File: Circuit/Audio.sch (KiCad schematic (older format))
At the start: 12 parts, among them U5 NAU8814

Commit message: BOM information to schematic. Power & main sheets mostly.
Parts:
- renumbered C17 to C?, C10 to C?
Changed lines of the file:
@@
 	1400 3900 1550 3900
 $Comp
-L C_Small C17
+L C_Small C?
 U 1 1 581FF4BD
 P 6950 3250
-F 0 "C17" H 6960 3320 50  0000 L CNN
+F 0 "C?" H 6960 3320 50  0000 L CNN
 F 1 "100pF" H 6960 3170 50  0000 L CNN
 F 2 "Capacitors_SMD:C_0603_HandSoldering" H 6950 3250 50  0001 C CNN
@@
 $EndComp
 $Comp
-L C_Small C10
+L C_Small C?
 U 1 1 5820032A
 P 6500 3000
-F 0 "C10" H 6510 3070 50  0000 L CNN
+F 0 "C?" H 6510 3070 50  0000 L CNN
 F 1 "100pF" H 6510 2920 50  0000 L CNN
 F 2 "Capacitors_SMD:C_0603_HandSoldering" H 6500 3000 50  0001 C CNN

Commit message: Updated alligator clips.
Some basic placement
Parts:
- gave numbers to parts that had none: 2
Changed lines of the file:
@@
 Connection ~ 1400 2450
 $Comp
-L +3.3V #PWR059
+L +3.3V #PWR056
 U 1 1 581BE27A
 P 5750 2750
-F 0 "#PWR059" H 5750 2600 50  0001 C CNN
+F 0 "#PWR056" H 5750 2600 50  0001 C CNN
 F 1 "+3.3V" H 5750 2890 50  0000 C CNN
 F 2 "" H 5750 2750 50  0000 C CNN
@@
 	2100 1900 2250 1900
 $Comp
-L GND #PWR060
+L GND #PWR057
 U 1 1 581BEFAA
 P 5750 2200
-F 0 "#PWR060" H 5750 1950 50  0001 C CNN
+F 0 "#PWR057" H 5750 1950 50  0001 C CNN
 F 1 "GND" H 5750 2050 50  0000 C CNN
 F 2 "" H 5750 2200 50  0000 C CNN
@@
 	800  2450 800  2050
 $Comp
-L GND #PWR061
+L GND #PWR058
 U 1 1 581BF41C
 P 7400 3850
-F 0 "#PWR061" H 7400 3600 50  0001 C CNN
+F 0 "#PWR058" H 7400 3600 50  0001 C CNN
 F 1 "GND" H 7400 3700 50  0000 C CNN
 F 2 "" H 7400 3850 50  0000 C CNN
@@
 Mono Out - NC or come out to header?\nOr could go to TRS 3.5mm jack.
 $Comp
-L GND #PWR062
+L GND #PWR059
 U 1 1 581BFD59
 P 4600 4450
-F 0 "#PWR062" H 4600 4200 50  0001 C CNN
+F 0 "#PWR059" H 4600 4200 50  0001 C CNN
 F 1 "GND" H 4600 4300 50  0000 C CNN
 F 2 "" H 4600 4450 50  0000 C CNN
@@
 Connection ~ 3850 3800
 $Comp
-L +3.3V #PWR063
+L +3.3V #PWR060
 U 1 1 581C0164
 P 3600 3600
-F 0 "#PWR063" H 3600 3450 50  0001 C CNN
+F 0 "#PWR060" H 3600 3450 50  0001 C CNN
 F 1 "+3.3V" H 3600 3740 50  0000 C CNN
 F 2 "" H 3600 3600 50  0000 C CNN
@@
 $EndComp
 $Comp
-L GND #PWR064
+L GND #PWR061
 U 1 1 581C01A1
 P 3850 4450
-F 0 "#PWR064" H 3850 4200 50  0001 C CNN
+F 0 "#PWR061" H 3850 4200 50  0001 C CNN
 F 1 "GND" H 3850 4300 50  0000 C CNN
 F 2 "" H 3850 4450 50  0000 C CNN
@@
 AUX input could go to DAC on ESP32..\nfor.. reasons?\nOr could go to TRS 3.5mm jack.
 $Comp
-L GND #PWR065
+L GND #PWR062
 U 1 1 581C0598
 P 5850 4700
-F 0 "#PWR065" H 5850 4450 50  0001 C CNN
+F 0 "#PWR062" H 5850 4450 50  0001 C CNN
 F 1 "GND" H 5850 4550 50  0000 C CNN
 F 2 "" H 5850 4700 50  0000 C CNN
@@
 	1400 3900 1550 3900
 $Comp
-L C_Small C?
+L C_Small C18
 U 1 1 581FF4BD
 P 6950 3250
-F 0 "C?" H 6960 3320 50  0000 L CNN
+F 0 "C18" H 6960 3320 50  0000 L CNN
 F 1 "100pF" H 6960 3170 50  0000 L CNN
 F 2 "Capacitors_SMD:C_0603_HandSoldering" H 6950 3250 50  0001 C CNN
@@
 $EndComp
 $Comp
-L C_Small C?
+L C_Small C17
 U 1 1 5820032A
 P 6500 3000
-F 0 "C?" H 6510 3070 50  0000 L CNN
+F 0 "C17" H 6510 3070 50  0000 L CNN
 F 1 "100pF" H 6510 2920 50  0000 L CNN
 F 2 "Capacitors_SMD:C_0603_HandSoldering" H 6500 3000 50  0001 C CNN

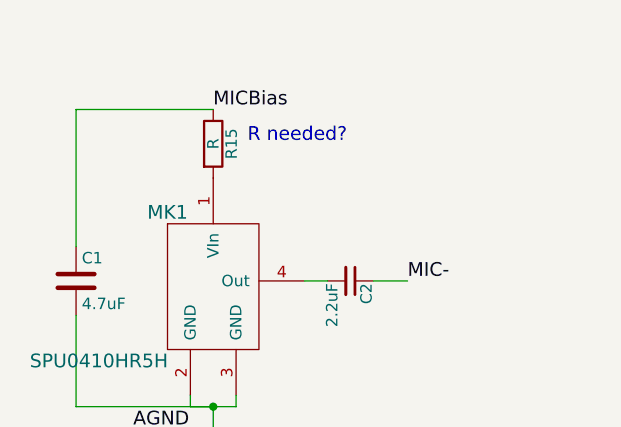
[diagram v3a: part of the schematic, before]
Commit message: Change to 3v3 regulator.
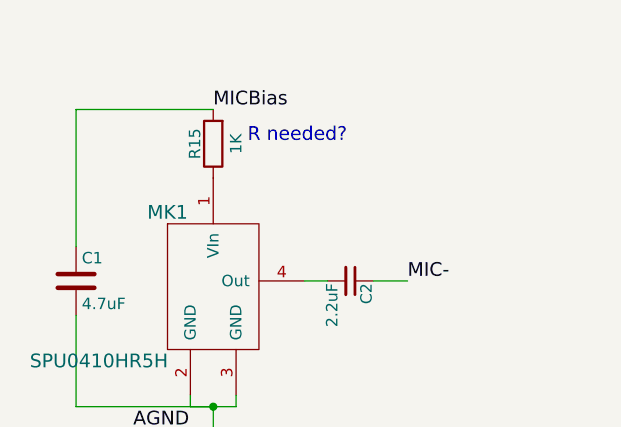
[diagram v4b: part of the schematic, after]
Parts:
- C2: footprint (none) -> Capacitors_SMD:C_0603_HandSoldering
- R15: value R -> 1K; footprint (none) -> Resistors_SMD:R_0603_HandSoldering; Digikey PN (none) -> 311-1.0KGRCT-ND; Link (none) -> http://www.digikey.com.au/product-detail/en/yageo/RC0603JR-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; Manufacturer PN (none) -> RC0603JR-071KL; Unit Cost (none) -> 0.10
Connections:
- net MICBias: now also R15.2; no longer R15.1
- net at MK1.1 (VIn): now also R15.1; no longer R15.2
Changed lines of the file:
@@
 LIBS:spu0410hr5h
 LIBS:ili9341.touchlcd.red
+LIBS:NCP5501
 LIBS:IoTuz-cache
 EELAYER 25 0
@@
 F 0 "C2" H 2010 1970 50  0000 L CNN
 F 1 "2.2uF" H 2010 1820 50  0000 L CNN
-F 2 "" H 2000 1900 50  0001 C CNN
+F 2 "Capacitors_SMD:C_0603_HandSoldering" H 2000 1900 50  0001 C CNN
 F 3 "" H 2000 1900 50  0000 C CNN
 F 4 "490-3296-1-ND" H 2000 1900 60  0001 C CNN "Digikey PN"
@@
 Text Label 1400 1150 0    60   ~ 0
 MICBias
-$Comp
-L R R15
-U 1 1 581BC437
-P 1400 1300
-F 0 "R15" V 1480 1300 50  0000 C CNN
-F 1 "R" V 1400 1300 50  0000 C CNN
-F 2 "" V 1330 1300 50  0001 C CNN
-F 3 "" H 1400 1300 50  0000 C CNN
-	1    1400 1300
-	1    0    0    -1
-$EndComp
 Wire Wire Line
 	5450 2700 5450 2900
@@
 Connection ~ 6500 3500
 Connection ~ 6500 3250
+$Comp
+L R R15
+U 1 1 5824B8C8
+P 1400 1300
+F 0 "R15" V 1480 1300 50  0000 C CNN
+F 1 "1K" V 1300 1300 50  0000 C CNN
+F 2 "Resistors_SMD:R_0603_HandSoldering" V 1330 1300 50  0001 C CNN
+F 3 "" H 1400 1300 50  0000 C CNN
+F 4 "311-1.0KGRCT-ND" V 1400 1300 60  0001 C CNN "Digikey PN"
+F 5 "http://www.digikey.com.au/product-detail/en/yageo/RC0603JR-071KL/311-1.0KGRCT-ND/729624" V 1400 1300 60  0001 C CNN "Link"
+F 6 "RC0603JR-071KL" V 1400 1300 60  0001 C CNN "Manufacturer PN"
+F 7 "0.10" V 1400 1300 60  0001 C CNN "Unit Cost"
+	1    1400 1300
+	-1   0    0    1
+$EndComp
 $EndSCHEMATC

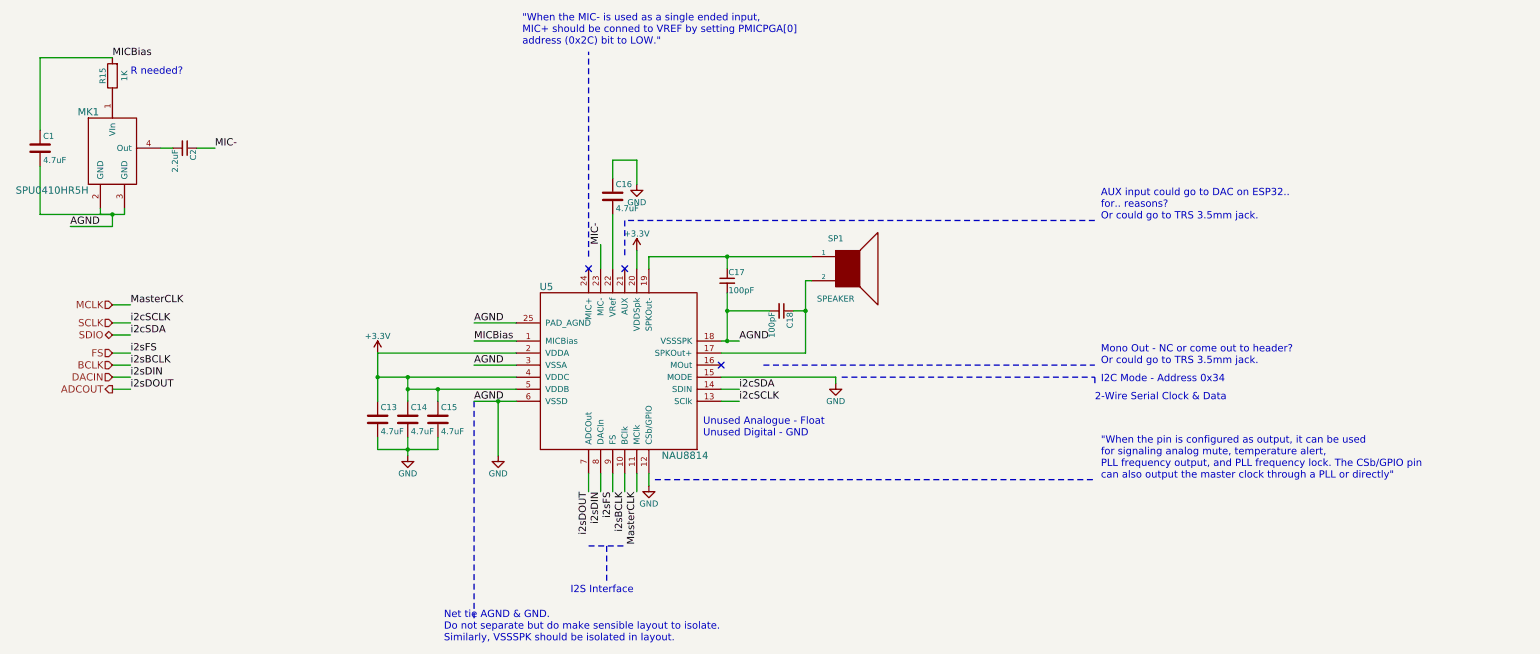
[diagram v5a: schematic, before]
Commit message: Changes to audio. Added 3.5mm TRS jack footprint.
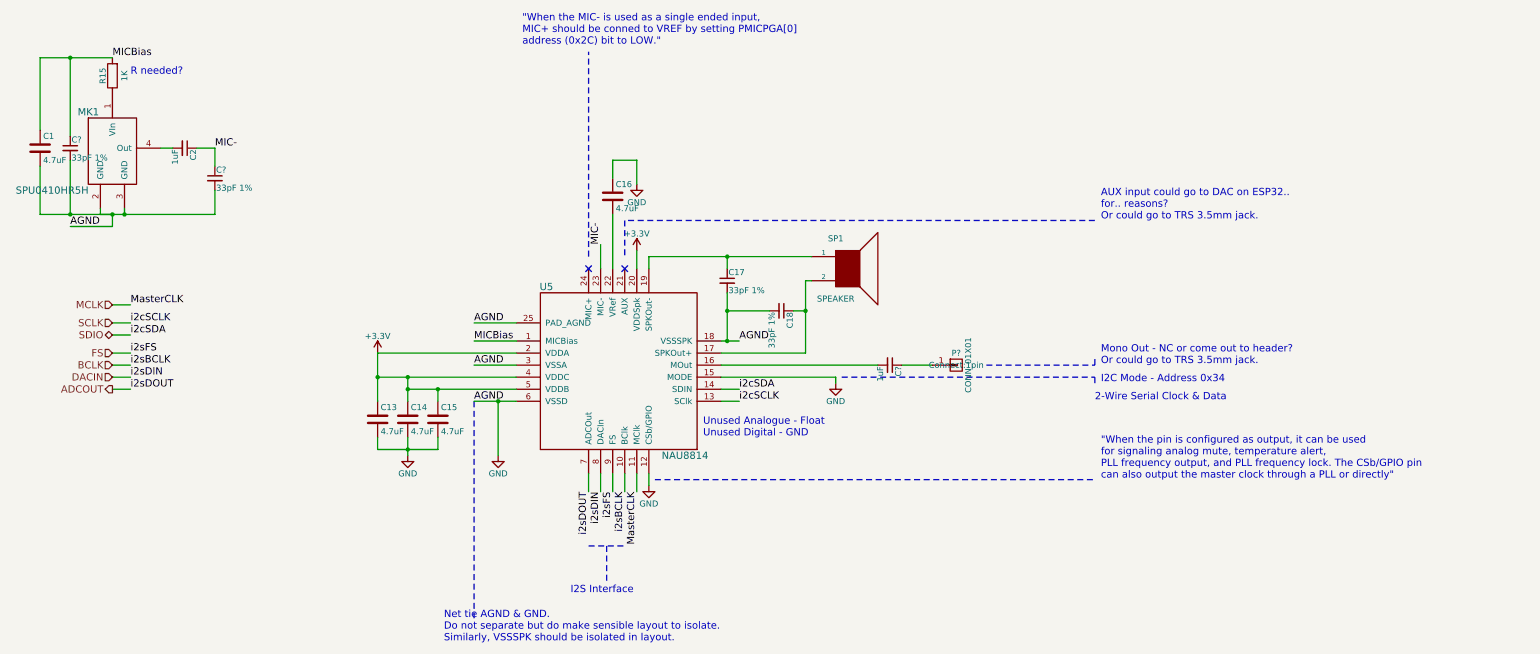
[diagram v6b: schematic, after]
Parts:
- added C? (x2): 33pF 1%, Capacitors_SMD:C_0603_HandSoldering, symbol C_Small
- added C?: 1uF, Capacitors_SMD:C_0603_HandSoldering, symbol C_Small
- added P?: CONN_01X01, Connect:1pin, symbol CONN_01X01
- C17, C18: value 100pF -> 33pF 1%; Digikey PN 490-3160-1-ND -> 1276-2262-1-ND; Link http://www.digikey.com.au/product-detail/en/murata-electron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 -> http://www.digikey.com.au/product-detail/en/samsung-electro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; Manufacturer PN GRM0335C1E101JA01D -> CL10C330FB8NNNC; Unit Cost 0.01 -> 0.14
- C2: value 2.2uF -> 1uF; Digikey PN 490-3296-1-ND -> 490-1536-1-ND; Link http://www.digikey.com.au/product-detail/en/murata-electronics-north-america/GRM188R61C225KE15D/490-3296-1-ND/702837 -> http://www.digikey.com.au/product-detail/en/murata-electronics-north-america/GRM188R61C105KA93D/490-1536-1-ND/587769; Manufacturer PN GRM188R61C225KE15D -> GRM188R61C105KA93D; Unit Cost 0.12 -> 0.1
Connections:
- net GND: now also C?.2, C?.2
- net MIC-: now also C?.1
- net MICBias: now also C?.1
- net at U5.16 (MOut): now also C?.2
- new net: C?.1, P?.1 (P1)
- no-connect marks 3 -> 2
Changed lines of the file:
@@
 P 2000 1900
 F 0 "C2" H 2010 1970 50  0000 L CNN
-F 1 "2.2uF" H 2010 1820 50  0000 L CNN
+F 1 "1uF" H 2010 1820 50  0000 L CNN
 F 2 "Capacitors_SMD:C_0603_HandSoldering" H 2000 1900 50  0001 C CNN
 F 3 "" H 2000 1900 50  0000 C CNN
-F 4 "490-3296-1-ND" H 2000 1900 60  0001 C CNN "Digikey PN"
-F 5 "http://www.digikey.com.au/product-detail/en/murata-electronics-north-america/GRM188R61C225KE15D/490-3296-1-ND/702837" H 2000 1900 60  0001 C CNN "Link"
-F 6 "GRM188R61C225KE15D" H 2000 1900 60  0001 C CNN "Manufacturer PN"
-F 7 "0.12" H 2000 1900 60  0001 C CNN "Unit Cost"
+F 4 "490-1536-1-ND" H 2000 1900 60  0001 C CNN "Digikey PN"
+F 5 "http://www.digikey.com.au/product-detail/en/murata-electronics-north-america/GRM188R61C105KA93D/490-1536-1-ND/587769" H 2000 1900 60  0001 C CNN "Link"
+F 6 "GRM188R61C105KA93D" H 2000 1900 60  0001 C CNN "Manufacturer PN"
+F 7 "0.1" H 2000 1900 60  0001 C CNN "Unit Cost"
 	1    2000 1900
 	0    1    1    0
@@
 	1300 2400 1300 2450
 Wire Wire Line
-	1300 2450 1500 2450
+	1300 2450 2250 2450
 Wire Wire Line
 	1400 2550 1400 2450
@@
 $EndComp
 Wire Wire Line
-	1400 1150 800  1150
+	800  1150 1400 1150
 Wire Wire Line
 	800  1150 800  1750
@@
 NoConn ~ 5650 2900
 Wire Wire Line
-	7200 2800 5850 2800
+	5850 2800 7200 2800
 Wire Wire Line
 	5850 2800 5850 2900
@@
 Wire Wire Line
 	7150 3600 6450 3600
-Wire Notes Line
-	6800 3700 9550 3700
 Text Notes 9600 3700 0    60   ~ 0
 Mono Out - NC or come out to header?\nOr could go to TRS 3.5mm jack.
@@
 $EndComp
 Wire Wire Line
-	3850 4450 3850 4300
+	3850 4300 3850 4450
 Wire Wire Line
 	3600 4400 4100 4400
@@
 Text Notes 9600 4650 0    60   ~ 0
 "When the pin is configured as output, it can be used\nfor signaling analog mute, temperature alert, \nPLL frequency output, and PLL frequency lock. The CSb/GPIO pin\ncan also output the master clock through a PLL or directly"
-NoConn ~ 6450 3700
 Text Notes 9550 4000 0    60   ~ 0
  2-Wire Serial Clock & Data
@@
 	1400 3900 1550 3900
 $Comp
-L C_Small C18
-U 1 1 581FF4BD
-P 6950 3250
-F 0 "C18" H 6960 3320 50  0000 L CNN
-F 1 "100pF" H 6960 3170 50  0000 L CNN
-F 2 "Capacitors_SMD:C_0603_HandSoldering" H 6950 3250 50  0001 C CNN
-F 3 "" H 6950 3250 50  0000 C CNN
-F 4 "490-3160-1-ND" H 6950 3250 60  0001 C CNN "Digikey PN"
-F 5 "http://www.digikey.com.au/product-detail/en/murata-electronics-north-america/GRM0335C1E101JA01D/490-3160-1-ND/702701" H 6950 3250 60  0001 C CNN "Link"
-F 6 "GRM0335C1E101JA01D" H 6950 3250 60  0001 C CNN "Manufacturer PN"
-F 7 "0.01" H 6950 3250 60  0001 C CNN "Unit Cost"
-	1    6950 3250
-	0    1    1    0
-$EndComp
-$Comp
 L C_Small C17
 U 1 1 5820032A
 P 6500 3000
 F 0 "C17" H 6510 3070 50  0000 L CNN
-F 1 "100pF" H 6510 2920 50  0000 L CNN
+F 1 "33pF 1%" H 6510 2920 50  0000 L CNN
 F 2 "Capacitors_SMD:C_0603_HandSoldering" H 6500 3000 50  0001 C CNN
 F 3 "" H 6500 3000 50  0000 C CNN
-F 4 "490-3160-1-ND" H 6500 3000 60  0001 C CNN "Digikey PN"
-F 5 "http://www.digikey.com.au/product-detail/en/murata-electronics-north-america/GRM0335C1E101JA01D/490-3160-1-ND/702701" H 6500 3000 60  0001 C CNN "Link"
-F 6 "GRM0335C1E101JA01D" H 6500 3000 60  0001 C CNN "Manufacturer PN"
-F 7 "0.01" H 6500 3000 60  0001 C CNN "Unit Cost"
+F 4 "1276-2262-1-ND" H 6500 3000 60  0001 C CNN "Digikey PN"
+F 5 "http://www.digikey.com.au/product-detail/en/samsung-electro-mechanics-america-inc/CL10C330FB8NNNC/1276-2262-1-ND/3890348" H 6500 3000 60  0001 C CNN "Link"
+F 6 "CL10C330FB8NNNC" H 6500 3000 60  0001 C CNN "Manufacturer PN"
+F 7 "0.14" H 6500 3000 60  0001 C CNN "Unit Cost"
 	1    6500 3000
 	1    0    0    -1
@@
 	-1   0    0    1
 $EndComp
+Wire Wire Line
+	1050 1150 1050 1800
+Connection ~ 1050 1150
+Wire Wire Line
+	1050 2000 1050 2450
+Connection ~ 1050 2450
+Connection ~ 1500 2450
+$Comp
+L C_Small C18
+U 1 1 582BA565
+P 6950 3250
+F 0 "C18" H 6960 3320 50  0000 L CNN
+F 1 "33pF 1%" H 6960 3170 50  0000 L CNN
+F 2 "Capacitors_SMD:C_0603_HandSoldering" H 6950 3250 50  0001 C CNN
+F 3 "" H 6950 3250 50  0000 C CNN
+F 4 "1276-2262-1-ND" H 6950 3250 60  0001 C CNN "Digikey PN"
+F 5 "http://www.digikey.com.au/product-detail/en/samsung-electro-mechanics-america-inc/CL10C330FB8NNNC/1276-2262-1-ND/3890348" H 6950 3250 60  0001 C CNN "Link"
+F 6 "CL10C330FB8NNNC" H 6950 3250 60  0001 C CNN "Manufacturer PN"
+F 7 "0.14" H 6950 3250 60  0001 C CNN "Unit Cost"
+	1    6950 3250
+	0    1    1    0
+$EndComp
+$Comp
+L C_Small C?
+U 1 1 582BA612
+P 1050 1900
+F 0 "C?" H 1060 1970 50  0000 L CNN
+F 1 "33pF 1%" H 1060 1820 50  0000 L CNN
+F 2 "Capacitors_SMD:C_0603_HandSoldering" H 1050 1900 50  0001 C CNN
+F 3 "" H 1050 1900 50  0000 C CNN
+F 4 "1276-2262-1-ND" H 1050 1900 60  0001 C CNN "Digikey PN"
+F 5 "http://www.digikey.com.au/product-detail/en/samsung-electro-mechanics-america-inc/CL10C330FB8NNNC/1276-2262-1-ND/3890348" H 1050 1900 60  0001 C CNN "Link"
+F 6 "CL10C330FB8NNNC" H 1050 1900 60  0001 C CNN "Manufacturer PN"
+F 7 "0.14" H 1050 1900 60  0001 C CNN "Unit Cost"
+	1    1050 1900
+	1    0    0    -1
+$EndComp
+$Comp
+L C_Small C?
+U 1 1 582BA791
+P 2250 2150
+F 0 "C?" H 2260 2220 50  0000 L CNN
+F 1 "33pF 1%" H 2260 2070 50  0000 L CNN
+F 2 "Capacitors_SMD:C_0603_HandSoldering" H 2250 2150 50  0001 C CNN
+F 3 "" H 2250 2150 50  0000 C CNN
+F 4 "1276-2262-1-ND" H 2250 2150 60  0001 C CNN "Digikey PN"
+F 5 "http://www.digikey.com.au/product-detail/en/samsung-electro-mechanics-america-inc/CL10C330FB8NNNC/1276-2262-1-ND/3890348" H 2250 2150 60  0001 C CNN "Link"
+F 6 "CL10C330FB8NNNC" H 2250 2150 60  0001 C CNN "Manufacturer PN"
+F 7 "0.14" H 2250 2150 60  0001 C CNN "Unit Cost"
+	1    2250 2150
+	1    0    0    -1
+$EndComp
+$Comp
+L C_Small C?
+U 1 1 582BA940
+P 7850 3700
+F 0 "C?" H 7860 3770 50  0000 L CNN
+F 1 "1uF" H 7860 3620 50  0000 L CNN
+F 2 "Capacitors_SMD:C_0603_HandSoldering" H 7850 3700 50  0001 C CNN
+F 3 "" H 7850 3700 50  0000 C CNN
+F 4 "490-1536-1-ND" H 7850 3700 60  0001 C CNN "Digikey PN"
+F 5 "http://www.digikey.com.au/product-detail/en/murata-electronics-north-america/GRM188R61C105KA93D/490-1536-1-ND/587769" H 7850 3700 60  0001 C CNN "Link"
+F 6 "GRM188R61C105KA93D" H 7850 3700 60  0001 C CNN "Manufacturer PN"
+F 7 "0.1" H 7850 3700 60  0001 C CNN "Unit Cost"
+	1    7850 3700
+	0    1    1    0
+$EndComp
+Wire Wire Line
+	6450 3700 7750 3700
+Wire Wire Line
+	2250 1900 2250 2050
+Wire Wire Line
+	2250 2450 2250 2250
+$Comp
+L CONN_01X01 P?
+U 1 1 582BB613
+P 8400 3700
+F 0 "P?" H 8400 3800 50  0000 C CNN
+F 1 "CONN_01X01" V 8500 3700 50  0000 C CNN
+F 2 "Connect:1pin" H 8400 3700 50  0000 C CNN
+F 3 "" H 8400 3700 50  0000 C CNN
+	1    8400 3700
+	1    0    0    -1
+$EndComp
+Wire Wire Line
+	7950 3700 8200 3700
+Wire Notes Line
+	8650 3700 9550 3700
+Wire Notes Line
+	9550 3700 9550 3650
 $EndSCHEMATC
